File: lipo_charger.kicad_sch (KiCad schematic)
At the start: 4 parts

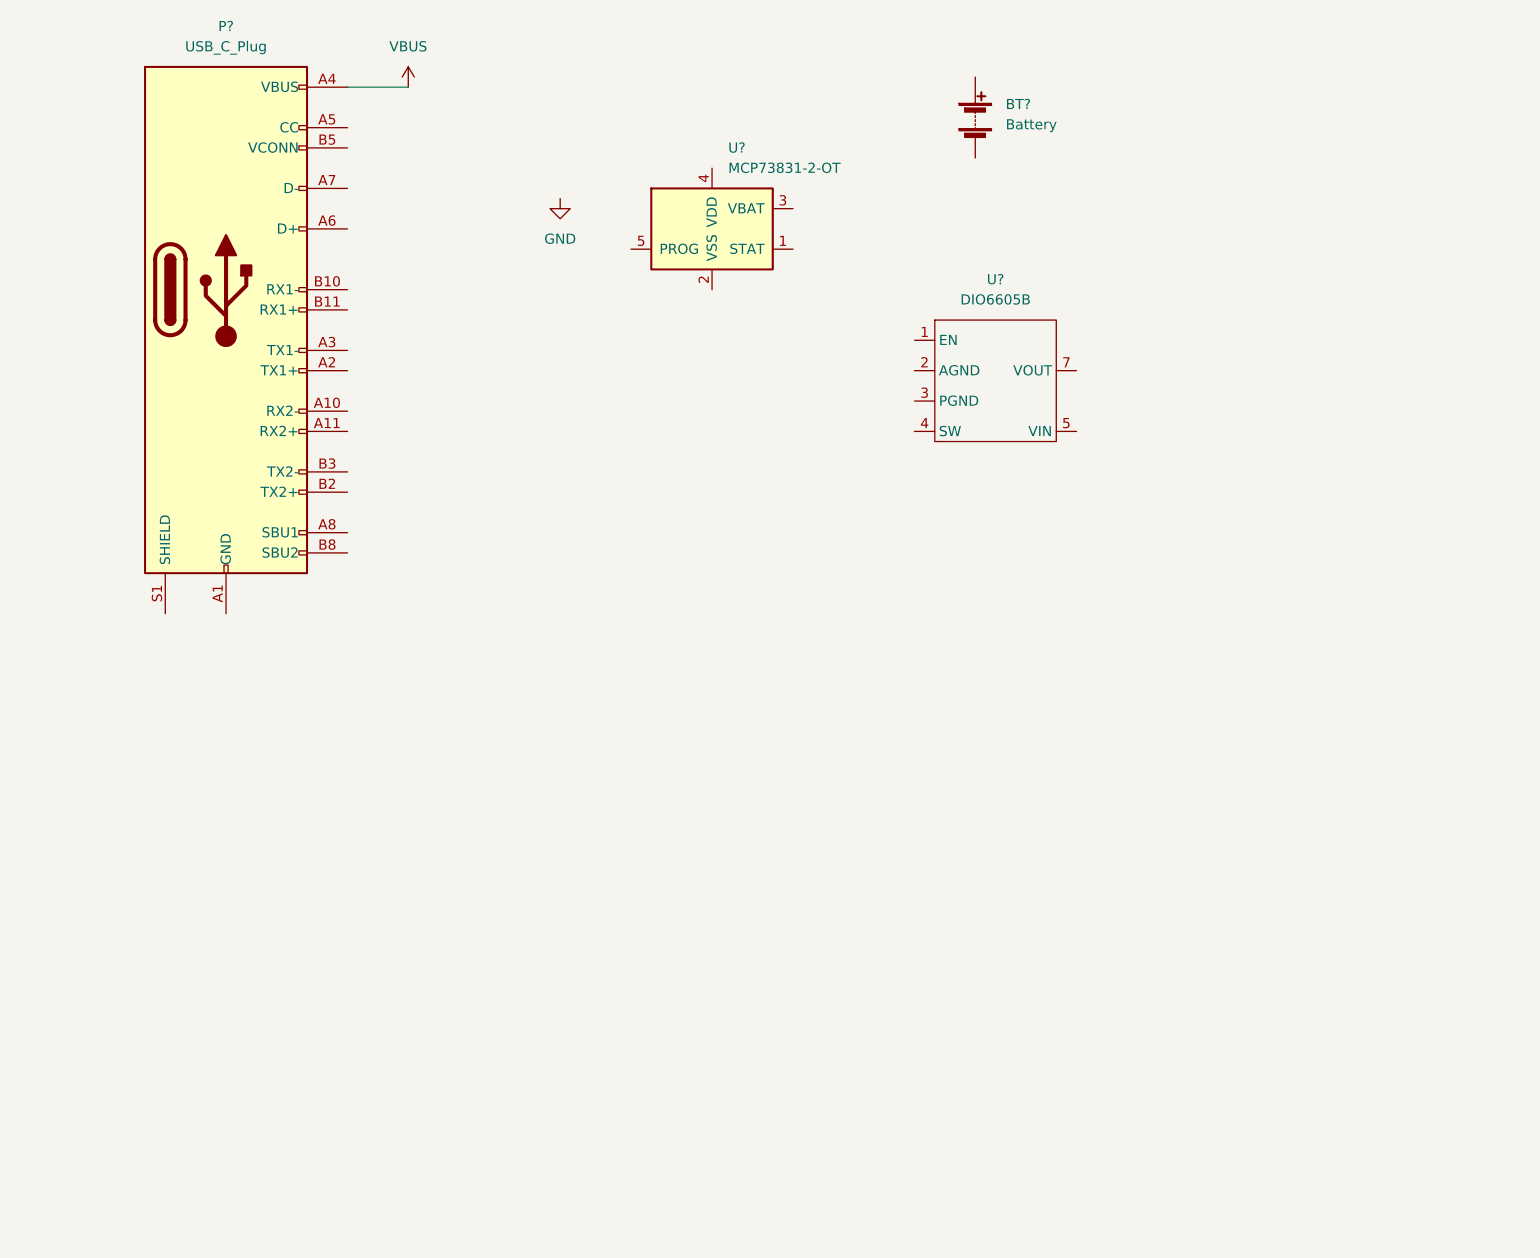
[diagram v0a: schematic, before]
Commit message: Finish first schematic draft
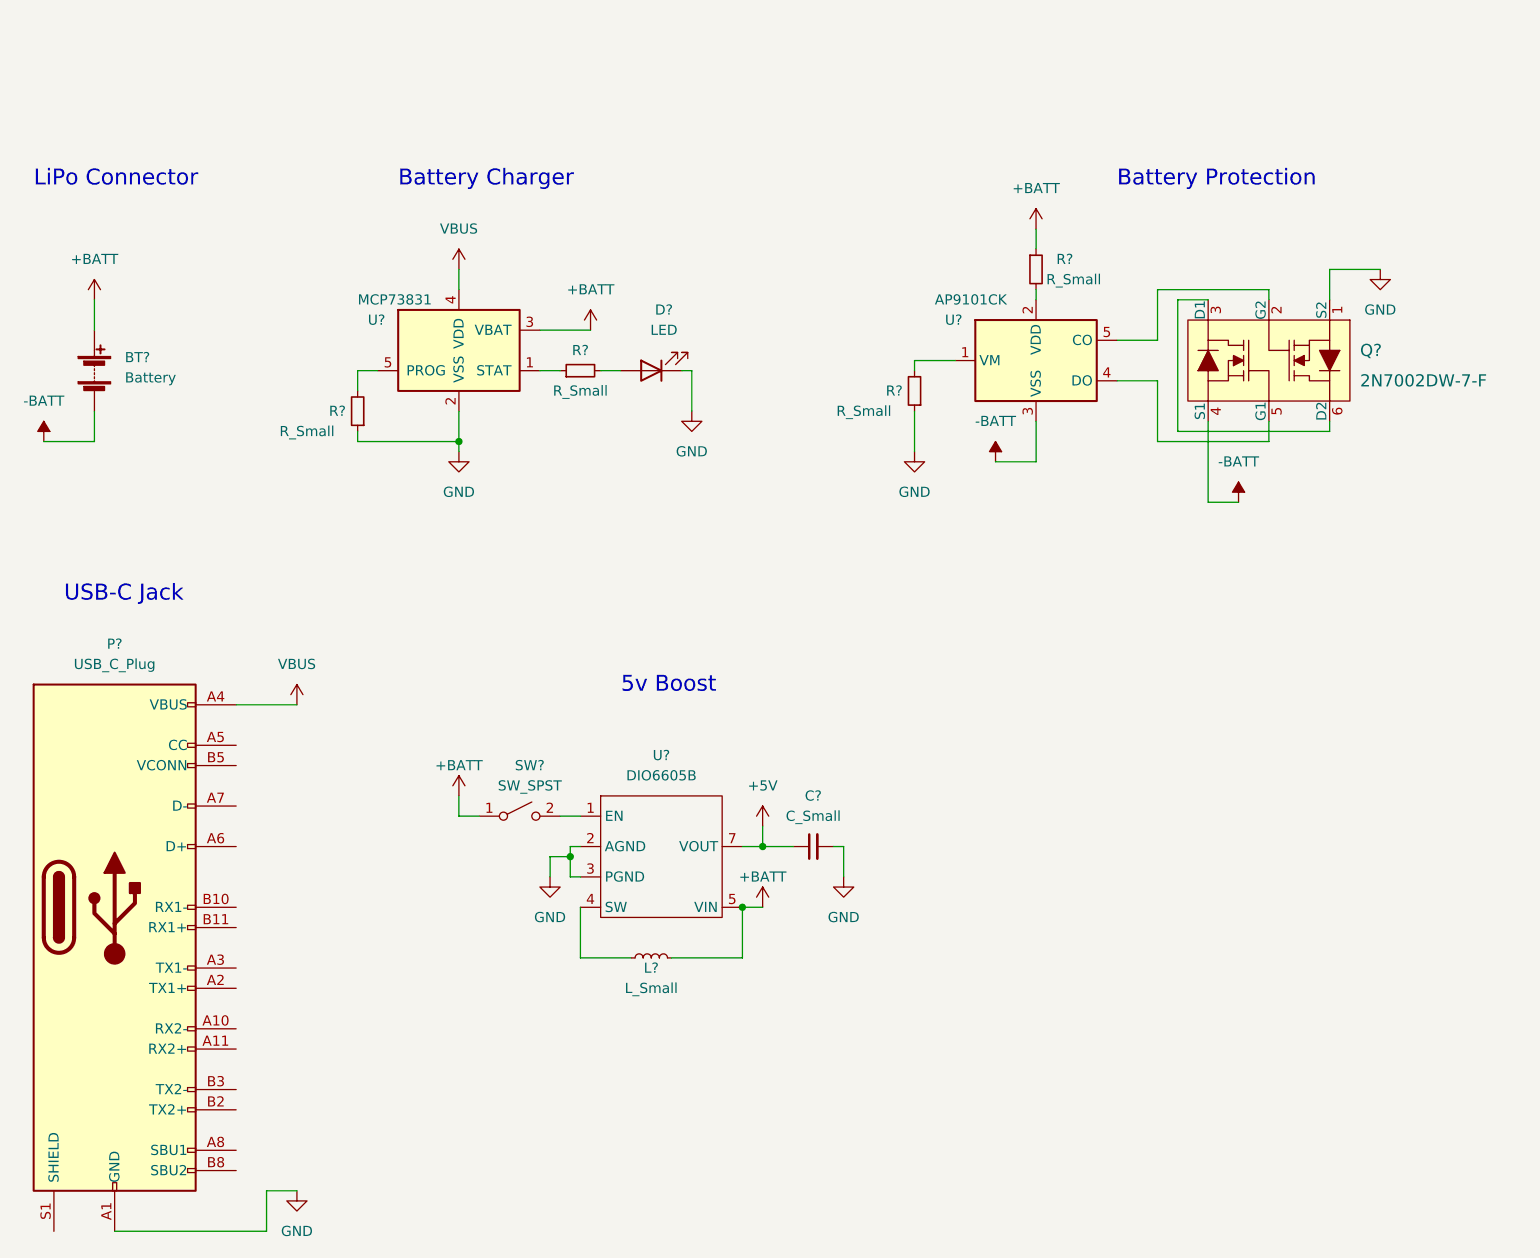
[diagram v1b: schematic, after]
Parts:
- added C?: C_Small, symbol Device:C_Small
- added D?: LED, symbol Device:LED
- added L?: L_Small, symbol Device:L_Small
- added Q?: 2N7002DW-7-F, digikey-footprints:SOT-363, symbol dk_Transistors-FETs-MOSFETs-Arrays:2N7002DW-7-F
- added R? (x4): R_Small, symbol Device:R_Small
- added SW?: SW_SPST, symbol Switch:SW_SPST
- added U?: AP9101CK, Package_TO_SOT_SMD:SOT-23-5, symbol Battery_Management:AP9101CK
- U?: value MCP73831-2-OT -> MCP73831
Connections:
- net GND: now also P?.A1 (GND), P?.A12 (GND), P?.B1 (GND), P?.B12 (GND), U?.2 (AGND), U?.2 (VSS), U?.3 (PGND), C?.2, D?.1 (K), Q?.1 (S2), R?.1, R?.1
- net VBUS: now also U?.4 (VDD)
- net at U?.1 (STAT): now also R?.1
- net +BATT: now reaches U?.3 (VBAT)
- net +BATT: now also BT?.1 (+), U?.5 (VIN), L?.2, R?.1, SW?.1 (A)
- net at U?.5 (PROG): now also R?.2
- net -BATT: now reaches BT?.2 (-)
- net -BATT: now also Q?.4 (S1), U?.3 (VSS)
- net at U?.1 (EN): now also SW?.2 (B)
- net at U?.4 (SW): now also L?.1
- net +5V: now reaches U?.7 (VOUT)
- net +5V: now also C?.1
- new net: Q?.2 (G2), U?.5 (CO)
- new net: Q?.3 (D1), Q?.6 (D2)
- new net: Q?.5 (G1), U?.4 (DO)
- new net: R?.2, U?.1 (VM)
- new net: D?.2 (A), R?.2
- new net: R?.2, U?.2 (VDD)
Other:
- note added: "5v Boost"
- note added: "Battery Charger"
- note added: "Battery Protection"
- note added: "LiPo Connector"
- note added: "USB-C Jack"
- moved on the sheet: BT?, P?, U?

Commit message: Add remaining passive components
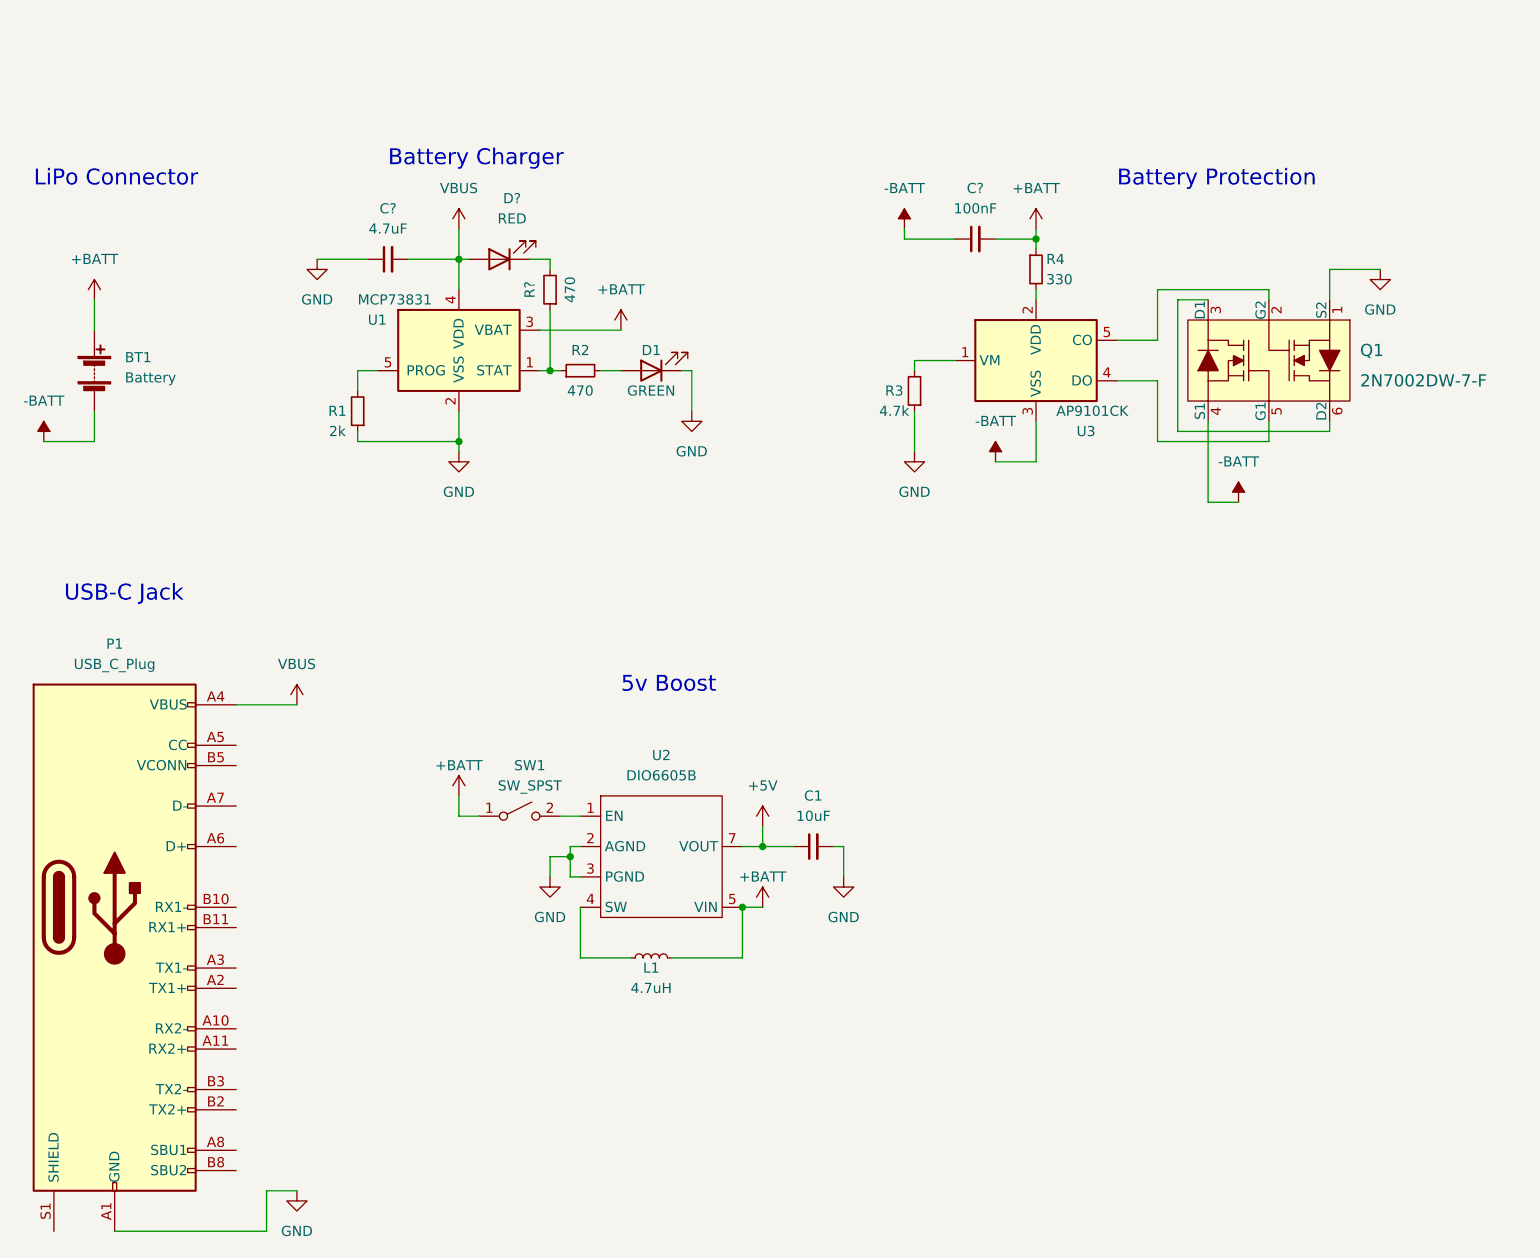
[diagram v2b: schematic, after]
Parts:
- added C?: 4.7uF, symbol Device:C_Small
- added C?: 100nF, symbol Device:C_Small
- added D?: RED, symbol Device:LED
- added R?: 470, symbol Device:R_Small
- C1: renamed from C?; value C_Small -> 10uF
- D1: renamed from D?; value LED -> GREEN
- L1: renamed from L?; value L_Small -> 4.7uH
- R1: renamed from R?; value R_Small -> 2k
- R2: renamed from R?; value R_Small -> 470
- R3: renamed from R?; value R_Small -> 4.7k
- R4: renamed from R?; value R_Small -> 330
- gave numbers to parts that had none: 7
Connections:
- net +BATT: now also C?.2
- net -BATT: now also C?.1
- net GND: now also C?.1
- net VBUS: now also C?.2, D?.2 (A)
- net at R2.1, U1.1 (STAT): now also R?.1
- new net: D?.1 (K), R?.2

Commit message: Place and route components
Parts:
- removed P1: USB_C_Plug, symbol Connector:USB_C_Plug
- added J1: USB_B_Micro, Connector_USB:USB_Micro-B_GCT_USB3076-30-A, symbol Connector:USB_B_Micro
- added J2: 22-23-2021, Connector_PinHeader_2.54mm:PinHeader_1x02_P2.54mm_Vertical, symbol dk_Rectangular-Connectors-Headers-Male-Pins:22-23-2021
- BT1: footprint (none) -> Connector_JST:JST_PH_B2B-PH-SM4-TB_1x02-1MP_P2.00mm_Vertical
- C1: footprint (none) -> Capacitor_SMD:C_0805_2012Metric
- C2, C3: renamed from C?; footprint (none) -> Capacitor_SMD:C_0805_2012Metric
- D1: footprint (none) -> LED_SMD:LED_0805_2012Metric
- D2: renamed from D?; footprint (none) -> LED_SMD:LED_0805_2012Metric
- L1: footprint (none) -> Inductor_SMD:L_0805_2012Metric
- R1, R3, R4: footprint (none) -> Resistor_SMD:R_0805_2012Metric_Pad1.20x1.40mm_HandSolder
- R2: value 470 -> 220; footprint (none) -> Resistor_SMD:R_0805_2012Metric_Pad1.20x1.40mm_HandSolder
- R5: renamed from R?; value 470 -> 220; footprint (none) -> Resistor_SMD:R_0805_2012Metric_Pad1.20x1.40mm_HandSolder
- SW1: value SW_SPST -> SW_SPDT; footprint (none) -> Button_Switch_THT:SW_Slide_1P2T_CK_OS102011MS2Q; symbol Switch:SW_SPST -> Switch:SW_SPDT
- U2: footprint (none) -> Package_DFN_QFN:DFN-8-1EP_3x2mm_P0.5mm_EP1.7x1.4mm
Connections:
- net +5V: now also J2.1
- net +BATT: now also SW1.2 (B); no longer SW1.1 (A)
- net GND: now also J1.5 (GND), J1.6 (Shield), J2.2
- net VBUS: now also J1.1 (VBUS)
- net at U2.1 (EN): now also SW1.3 (C); no longer SW1.2 (B)
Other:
- note added: "5v Output Headers"
- note added: "Micro USB Jack"
- note removed: "USB-C Jack"
